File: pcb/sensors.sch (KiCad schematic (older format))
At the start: 0 parts

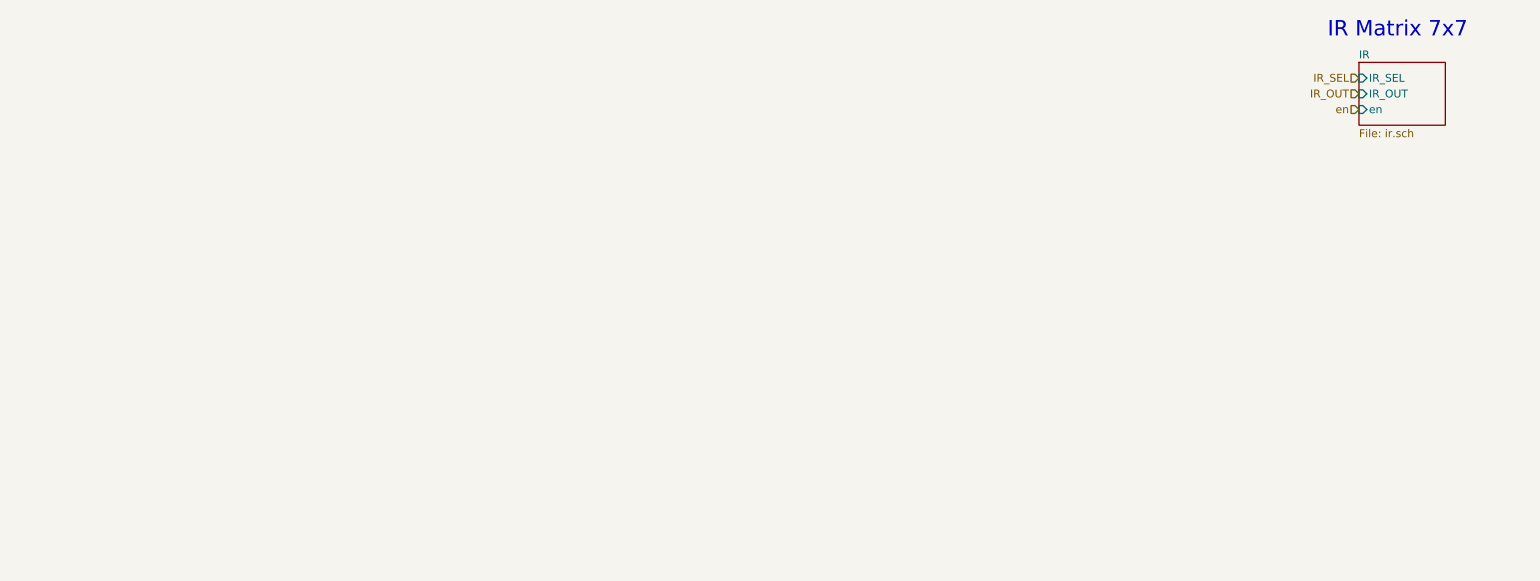
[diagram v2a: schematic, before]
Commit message: MCU connections, OLED and Sonar
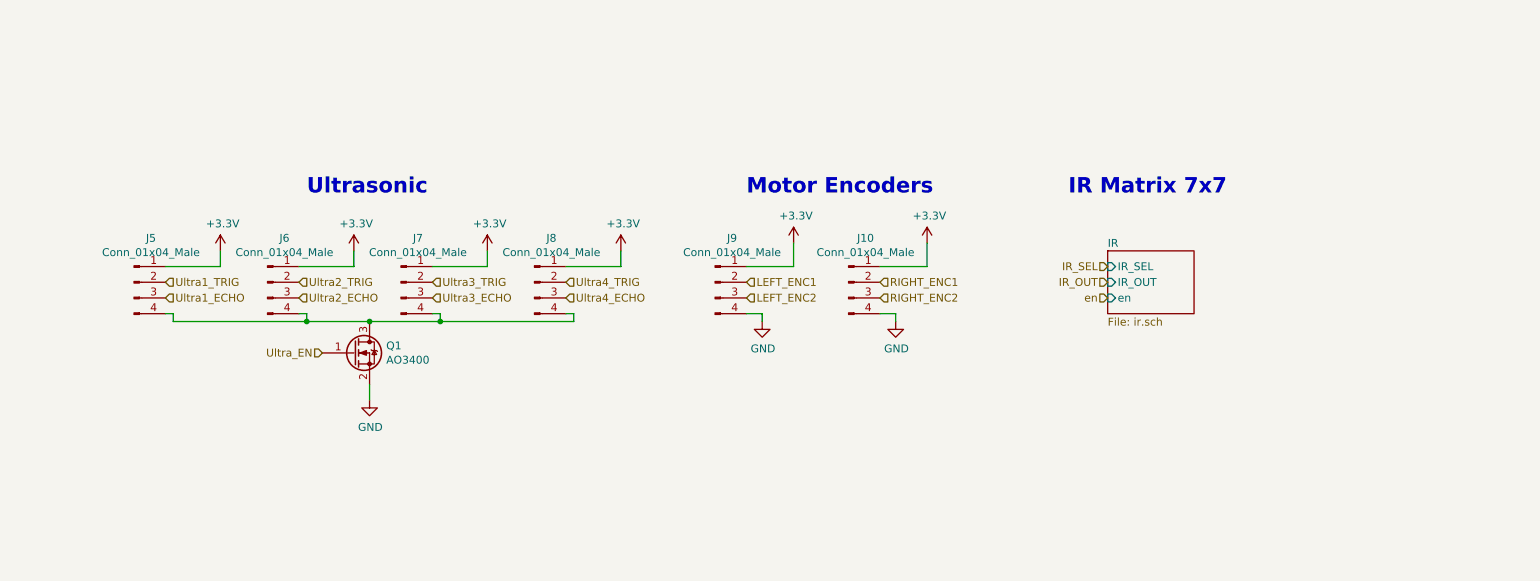
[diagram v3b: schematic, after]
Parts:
- added J10, J5, J6, J7, J8, J9: Conn_01x04_Male, Connector_PinHeader_2.54mm:PinHeader_1x04_P2.54mm_Vertical, symbol Connector:Conn_01x04_Male
- added Q1: AO3400, Package_TO_SOT_SMD:SOT-23, symbol rasbot:AO3400
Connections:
- new net: J5.4 (Pin_4), J6.4 (Pin_4), J7.4 (Pin_4), J8.4 (Pin_4), Q1.3 (D)
- new net +3V3: J10.1 (Pin_1), J5.1 (Pin_1), J6.1 (Pin_1), J7.1 (Pin_1), J8.1 (Pin_1), J9.1 (Pin_1)
- new net GND: J10.4 (Pin_4), J9.4 (Pin_4), Q1.2 (S)
- new net LEFT_ENC1: J9.2 (Pin_2)
- new net LEFT_ENC2: J9.3 (Pin_3)
- new net RIGHT_ENC1: J10.2 (Pin_2)
- new net RIGHT_ENC2: J10.3 (Pin_3)
- new net Ultra1_ECHO: J5.3 (Pin_3)
- new net Ultra1_TRIG: J5.2 (Pin_2)
- new net Ultra2_ECHO: J6.3 (Pin_3)
- new net Ultra2_TRIG: J6.2 (Pin_2)
- new net Ultra3_ECHO: J7.3 (Pin_3)
- new net Ultra3_TRIG: J7.2 (Pin_2)
- new net Ultra4_ECHO: J8.3 (Pin_3)
- new net Ultra4_TRIG: J8.2 (Pin_2)
- new net Ultra_EN: Q1.1 (G)
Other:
- note added: "Motor Encoders"
- note added: "Ultrasonic"

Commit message: Connect Ultrasonic Sensors
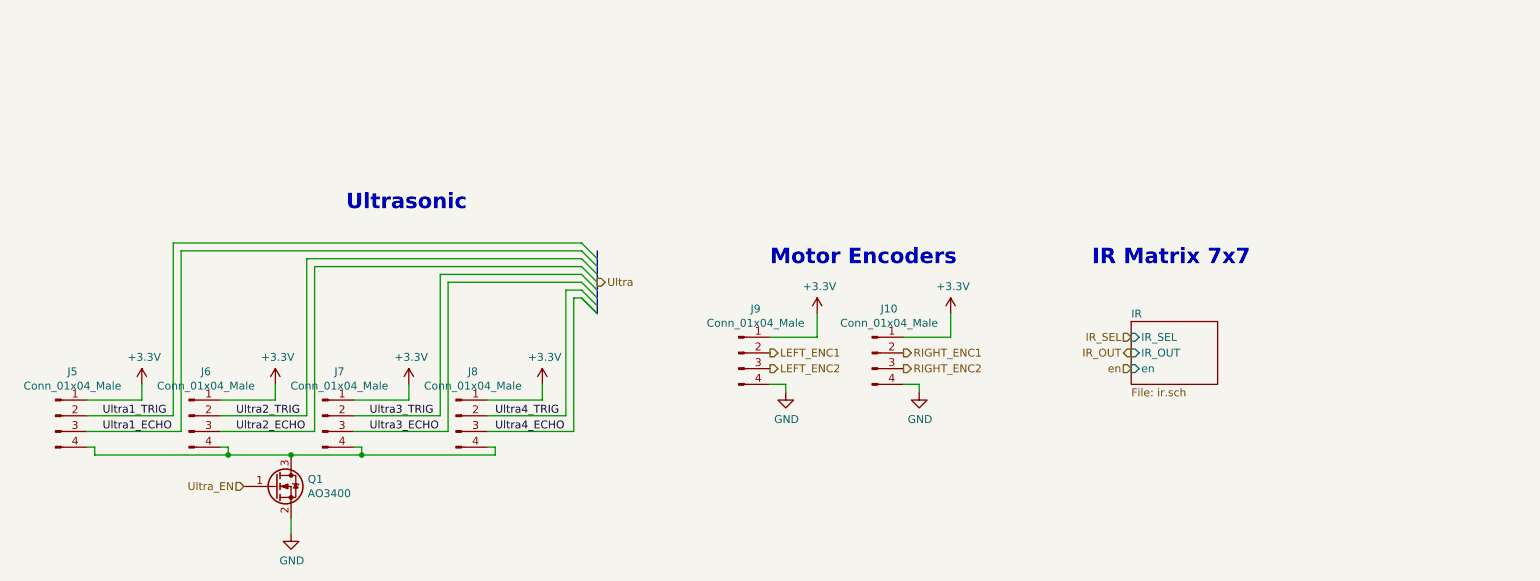
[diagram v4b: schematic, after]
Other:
- moved on the sheet: J10, J5, J6, J7, J8, J9, Q1
